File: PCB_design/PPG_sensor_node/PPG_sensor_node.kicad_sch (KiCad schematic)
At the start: 61 parts, among them J1 Conn_01x04_Socket, J2 Conn_01x04_Pin, J3 USB_C_Receptacle_USB2.0_16P, Q1 NMOS, Q2 NMOS, SW1 SW_SPST, SW2 SW_SPST, SW3 SW_SPST, U1 ESP32-C3, U2 LIS2DE12, U3 DW01A, U3 MAX17263xxTE, U5 TPS22917LDBV, U7 TLV75533PDBV, Y1 Crystal_GND24

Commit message: Split into two sensor file
split into ppg and acc file. draw the rect for better view. next to do is design usb/battery power adaption
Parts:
- removed C10: 10n, symbol Device:C
- removed U2: LIS2DE12, Package_LGA:LGA-12_2x2mm_P0.5mm, symbol Sensor_Motion:LIS2DE12
- added C4, C5: 1u, symbol Device:C
- added U4: MAX30102, OptoDevice:Maxim_OLGA-14_3.3x5.6mm_P0.8mm, symbol Sensor:MAX30102
- added U6: TPS78218DDC, Package_TO_SOT_SMD:SOT-23-5, symbol Regulator_Linear:TPS78218DDC
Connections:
- net 3.3V: now also C4.1, U4.10 (VLED+), U4.9 (VLED+), U6.1 (IN), U6.3 (EN)
- net GND: now also C4.2, C5.2, U4.12 (GND), U4.4 (PGND), U6.2 (GND), U6.4 (GND)
- net SCL: now also U4.2 (SCL)
- net SDA: now also U4.3 (SDA)
- new net: C5.1, U4.11 (VDD), U6.5 (OUT)
- no-connect marks 6 -> 5
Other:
- note added: "PPG IC"
- note removed: "ACC IC"
- moved on the sheet: AE1, C1, C11, C12, C13, C14, C15, C2, C20, C21, C22, C3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

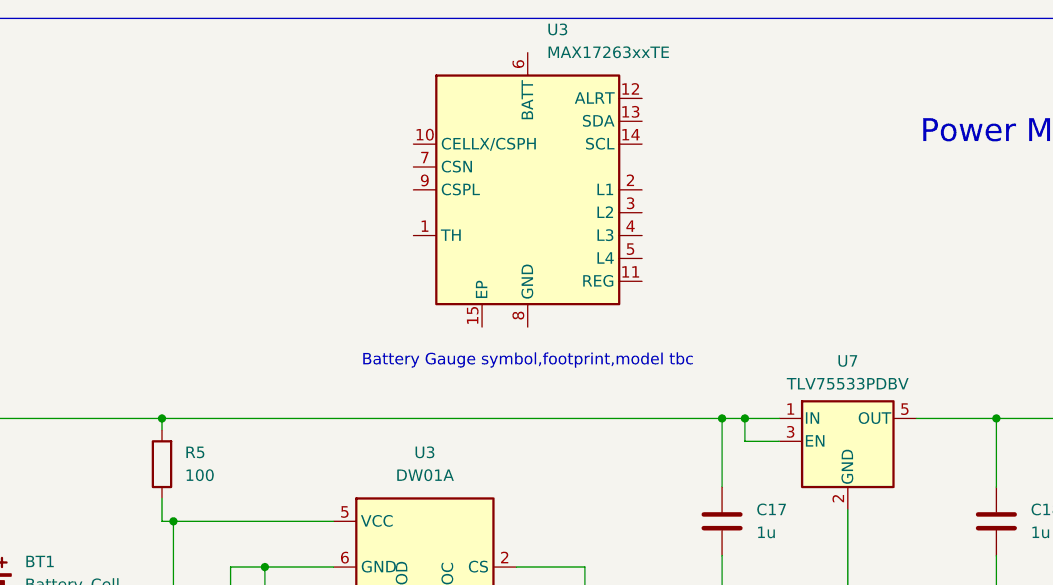
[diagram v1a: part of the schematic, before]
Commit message: update
choose a appropriate fuel gauge and draw the correspond symbol to add it into power management system for both two pcb file
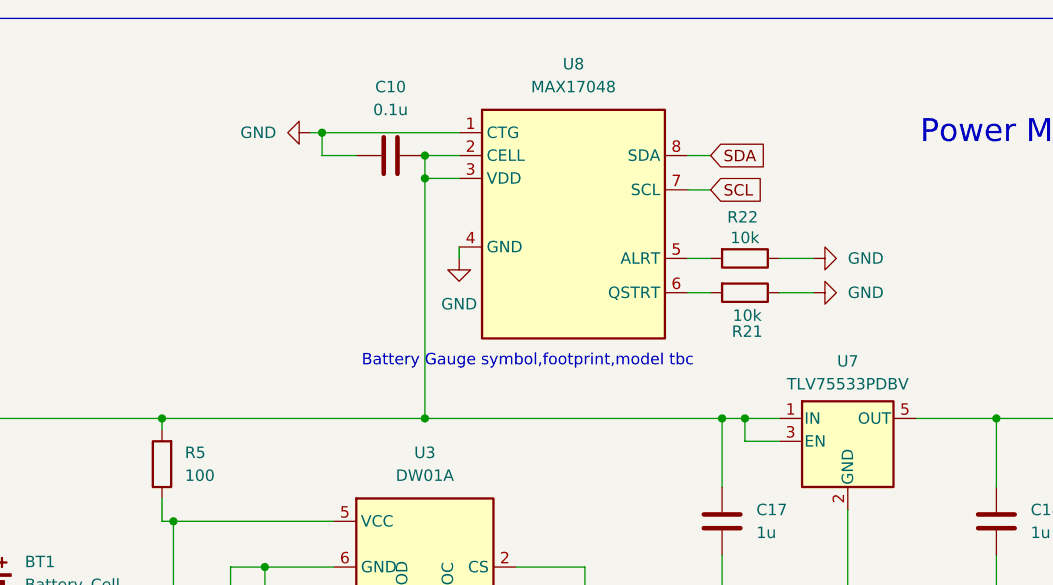
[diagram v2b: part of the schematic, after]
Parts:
- removed U3: MAX17263xxTE, Package_DFN_QFN:DFN-14-1EP_3x3mm_P0.4mm_EP1.78x2.35mm, symbol Battery_Management:MAX17263xxTE
- added C10: 0.1u, symbol Device:C
- added R21, R22: 10k, symbol Device:R
- added U8: MAX17048, Package_DFN_QFN:TDFN-8-1EP_2x2mm_P0.5mm_EP0.8x1.2mm, symbol symlib:MAX17048
- Y1: footprint (none) -> Crystal:Crystal_SMD_SeikoEpson_TSX3225-4Pin_3.2x2.5mm_HandSoldering
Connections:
- net GND: now also C10.1, R21.1, R22.1, U8.1 (CTG), U8.4 (GND)
- net SCL: now also U8.7 (SCL)
- net SDA: now also U8.8 (SDA)
- net at BT1.1 (+), C17.1, R5.2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: now also C10.2, U8.2 (CELL), U8.3 (VDD)
- new net: R21.2, U8.6 (QSTRT)
- new net: R22.2, U8.5 (ALRT)

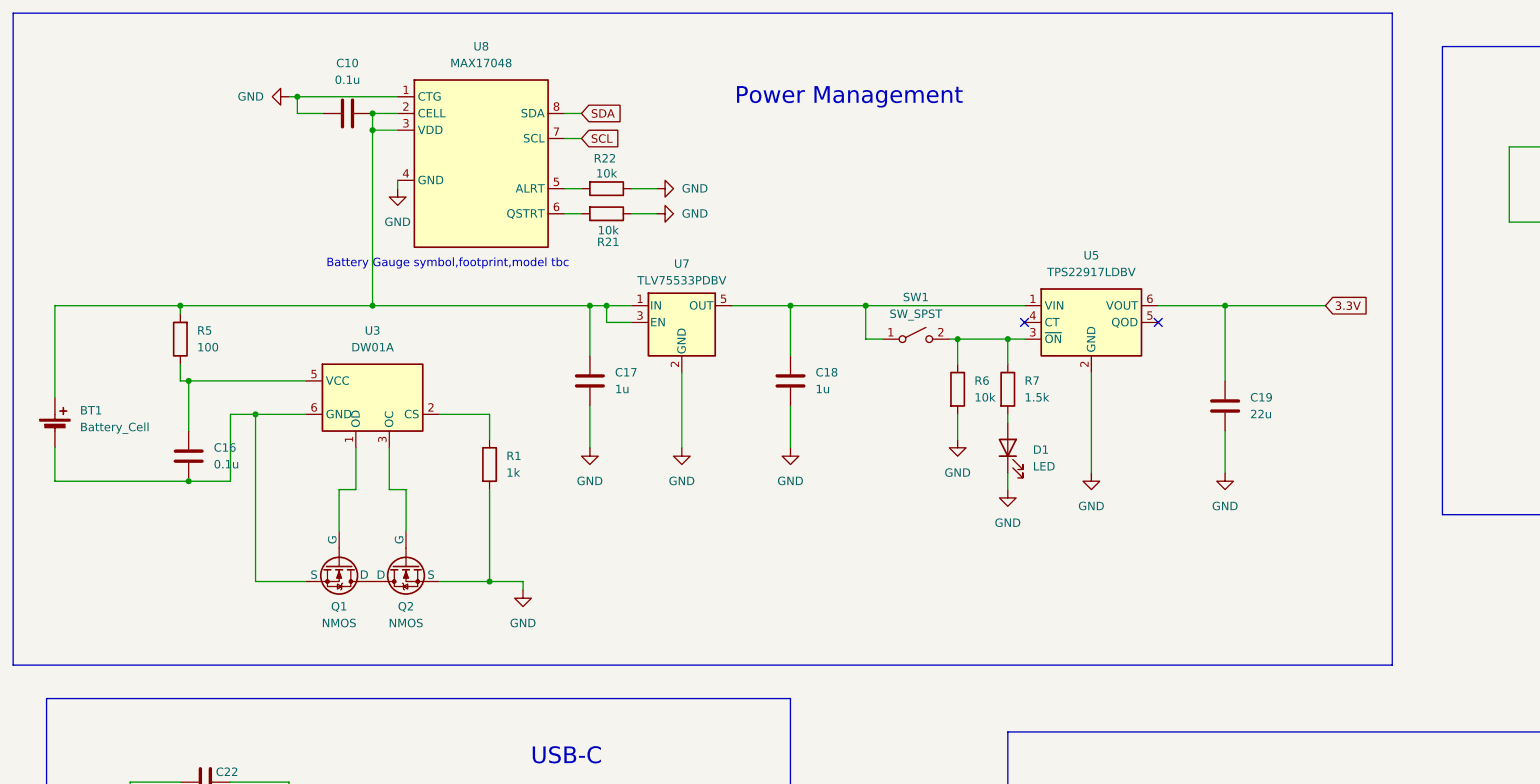
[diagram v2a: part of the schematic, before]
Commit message: update
add the ceramic parallel capacitor for driving ESP32 at big current
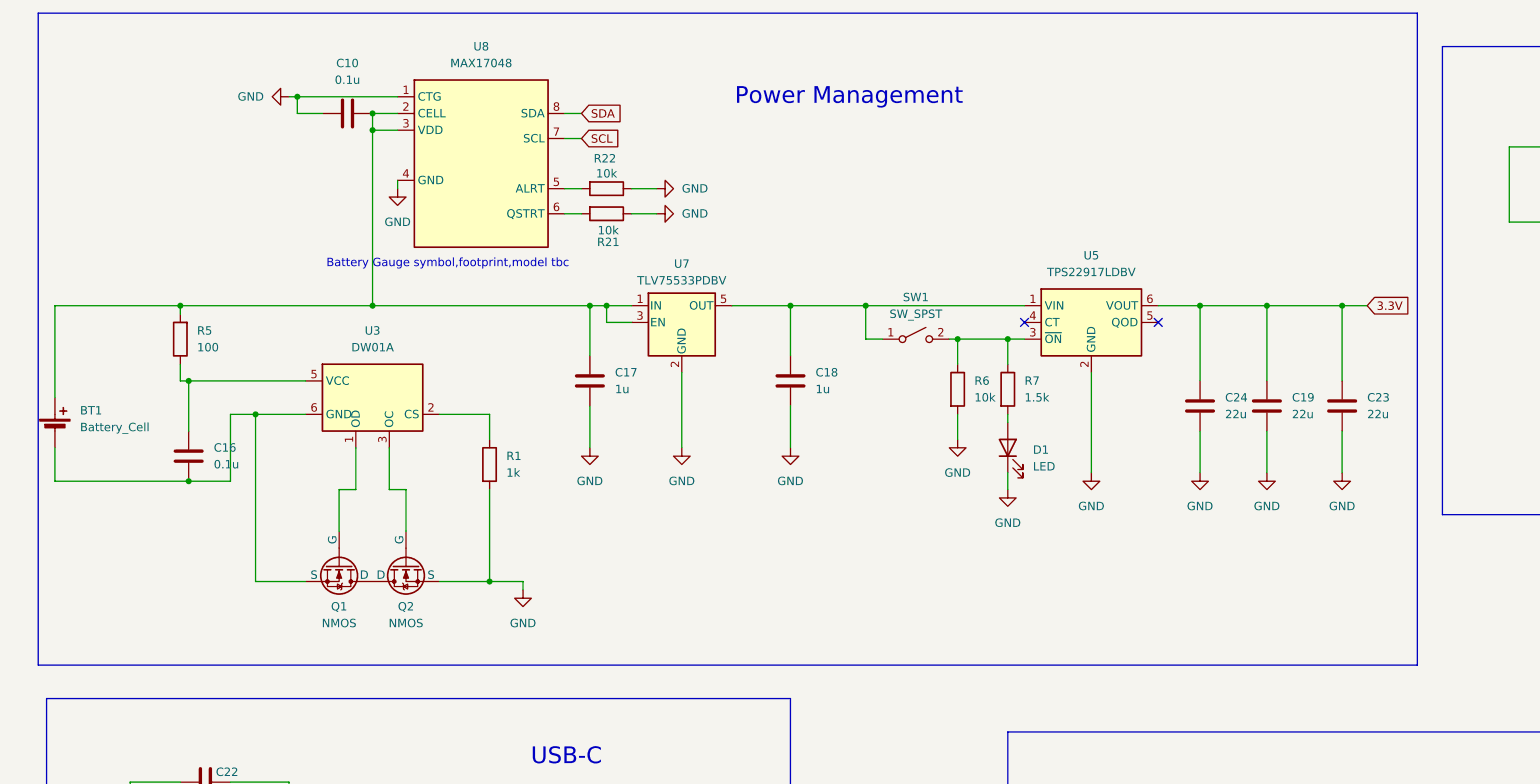
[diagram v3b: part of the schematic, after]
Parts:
- added C23, C24: 22u, symbol Device:C
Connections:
- net 3.3V: now also C23.1, C24.1
- net GND: now also C23.2, C24.2
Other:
- moved on the sheet: C19

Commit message: applied LTC4412 to both file
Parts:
- added D3: D_Schottky, symbol Device:D_Schottky
- added Q3: PMOS, symbol Simulation_SPICE:PMOS
- added U2: LTC4412xS6, Package_TO_SOT_SMD:TSOT-23-6, symbol Power_Management:LTC4412xS6
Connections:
- net GND: now also U2.2 (GND), U2.3 (CTL)
- net Vbus: now also D3.2 (A)
- net at BT1.1 (+), C10.2, R5.2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: now also Q3.1 (D), U2.1 (VIN); no longer C17.1, U7.1 (IN), U7.3 (EN)
- new net: C17.1, D3.1 (K), Q3.3 (S), U2.6 (SENSE), U7.1 (IN), U7.3 (EN)
- new net: Q3.2 (G), U2.5 (GATE)
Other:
- moved on the sheet: C17, C18, C19, C23, C24, C4, C5, D1, R6, R7, SW1, U4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

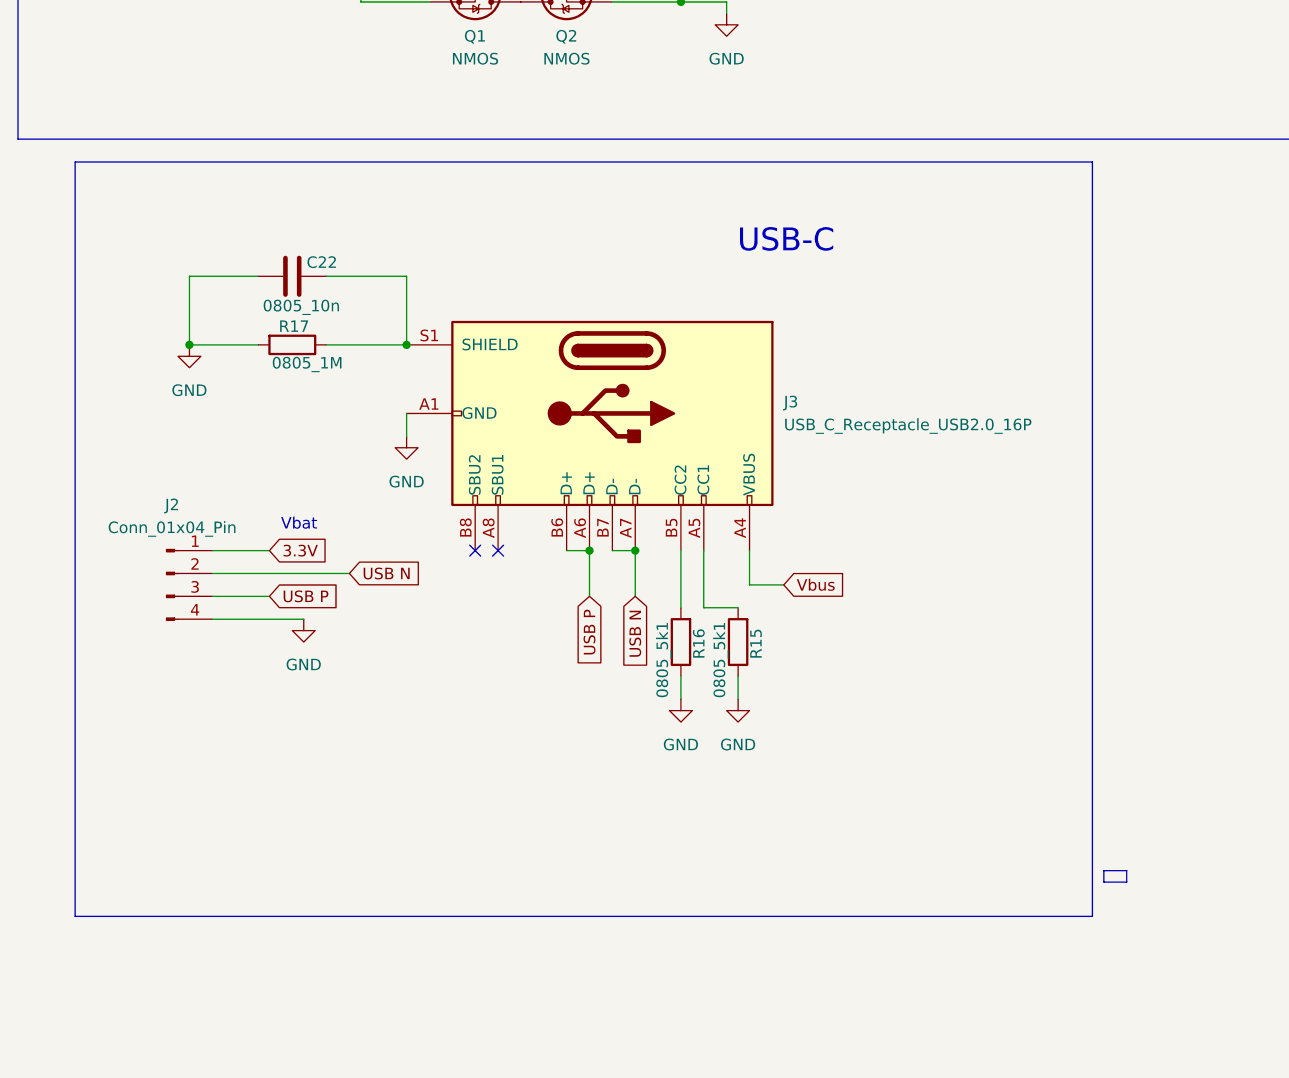
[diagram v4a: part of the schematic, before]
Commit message: quick update
split USBC into an individual file
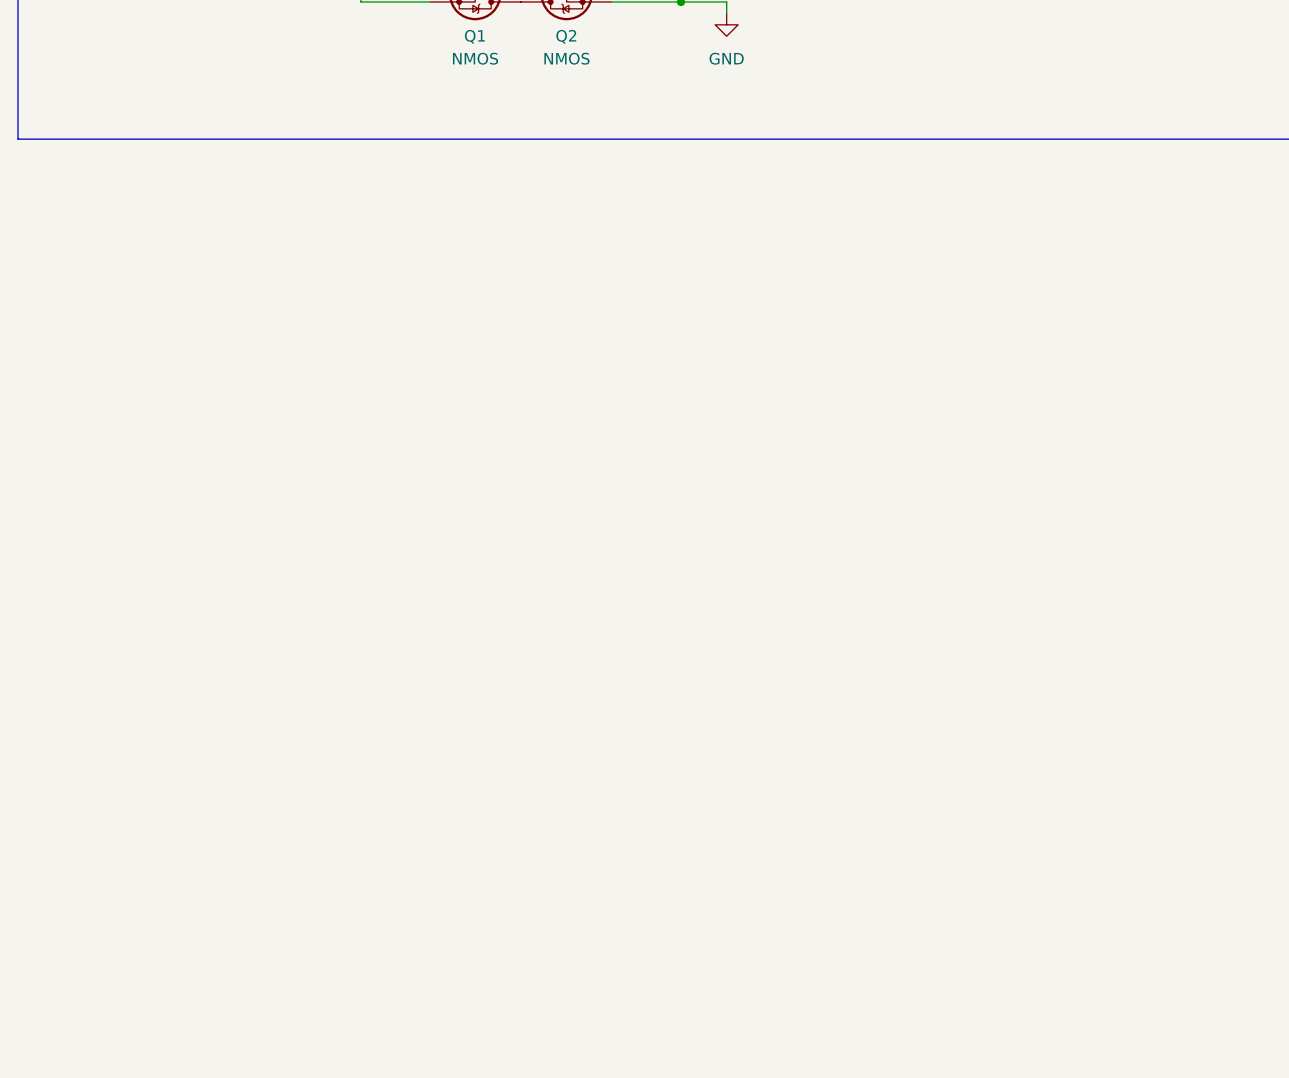
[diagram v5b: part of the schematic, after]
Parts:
- removed C22: 0805_10n, symbol Device:C
- removed J2: Conn_01x04_Pin, symbol Connector:Conn_01x04_Pin
- removed J3: USB_C_Receptacle_USB2.0_16P, symbol Connector:USB_C_Receptacle_USB2.0_16P
- removed R15, R16: 0805_5k1, symbol Device:R
- removed R17: 0805_1M, symbol Device:R
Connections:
- no-connect marks 5 -> 3
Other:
- note removed: "USB-C"
